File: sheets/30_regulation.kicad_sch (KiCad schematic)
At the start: 25 parts, among them U301 TPS62A02QDRLRQ1, U302 LP5907QMFX-3.3Q1

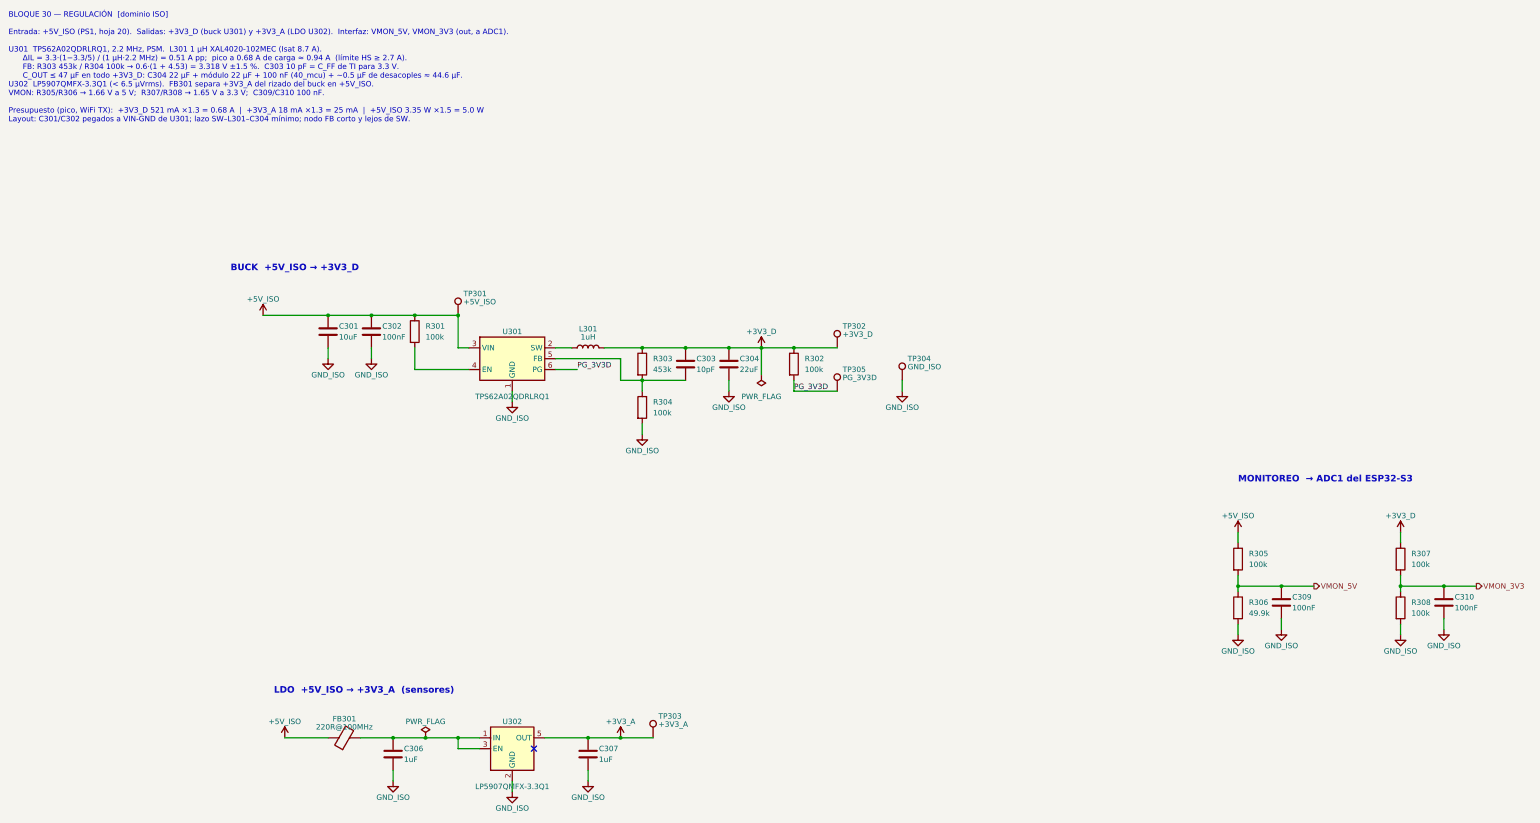
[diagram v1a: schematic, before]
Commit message: [Claude Code] 20_buck_5v: opción B (no aislada) con LMR38010; masas unificadas
- sheets/20_isolation -> sheets/20_buck_5v: se quitan PS201, ISO7763 y
  TPS7A1650; U201 LMR38010SQDDARQ1 (PROTO: LMR38010SDDAR, LCSC C5219310),
  5.02 V / 1 A a 400 kHz según TI SNVSC73B (L201 XAL6060-333, 3 x 22 uF,
  RT 64.9k, FB 100k/24.9k). Huella oficial HSOIC-8 con vías térmicas.
- Símbolo LMR38010 (easyeda2kicad) en lib/easyeda2kicad/INCLI-VA_easyeda,
  con tipos de pin ajustados; registrado en sym-lib-table.
- Todas las hojas: GND_ISO -> GND_VEH, +5V_ISO -> +5V_VEH.
- Raíz: EN/DIAG/FLT directos entre las hojas 40, 70 y 10; la hoja 20 sin pines.
- 10_power_input: R111 a +3V3_D, C109 = 100 nF (inrush con C105),
  C105 DNP solo en PROTO; se quita un PWR_FLAG suelto en GND_VEH.
- 70_output_ch: cambios de layout del usuario (hechos en KiCad).
- Textos de las hojas 30/40/50/80 y la raíz sin referencias al aislamiento.
- ERC: 0 en 10, 20, 30, 40, 50, 60 y 70; quedan los de 80 (hoja vacía).

Co-Authored-By: Claude Opus 5.5 <noreply@anthropic.com>
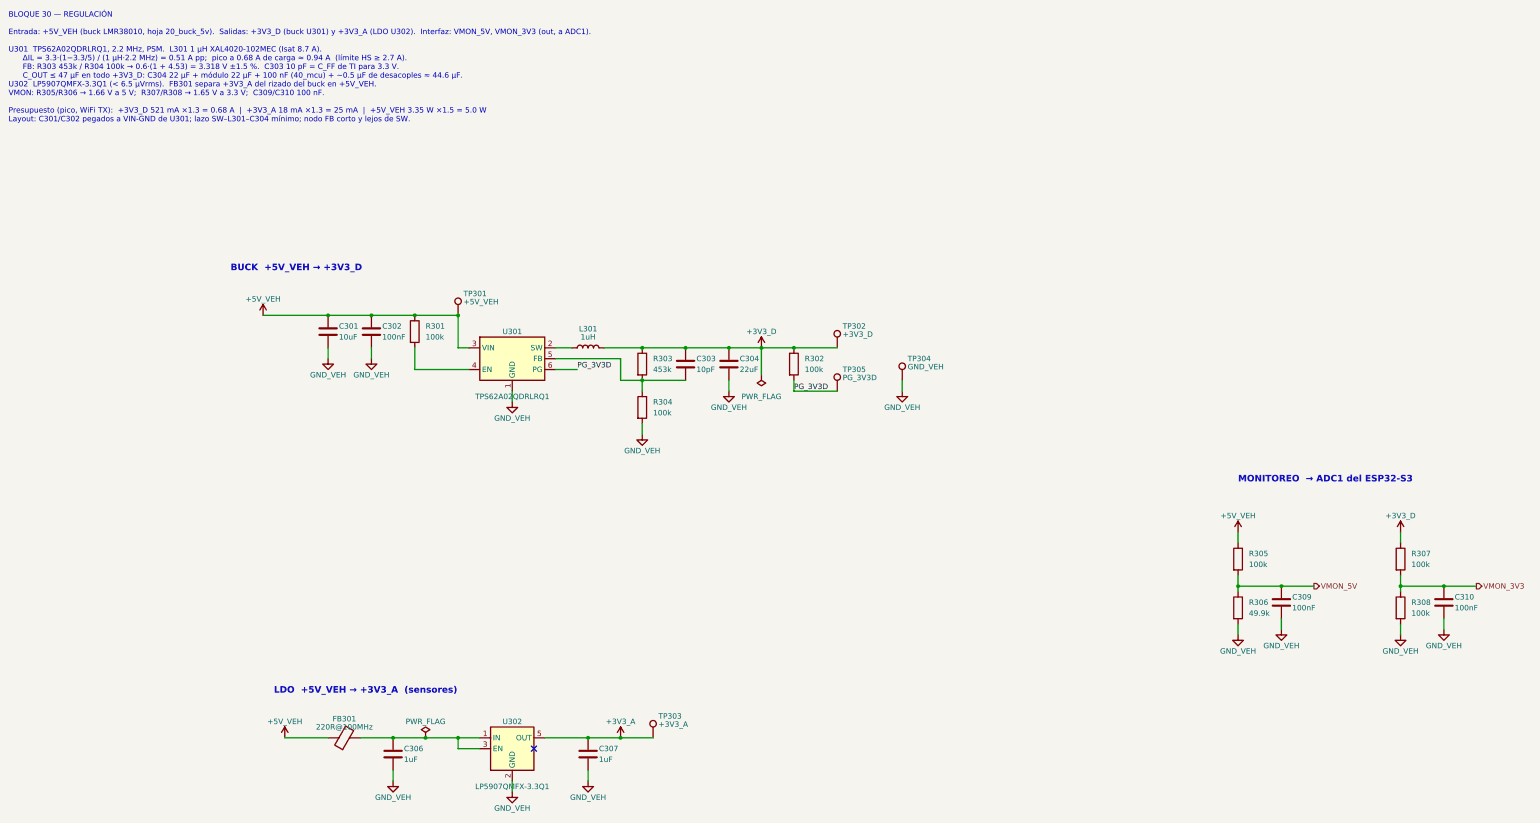
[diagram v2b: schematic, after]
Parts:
- FB301: Notes Aísla la entrada del LDO del rizado que el buck inyecta en +5V_ISO. 1.4 A, ~25 mA de carga. MPN a verificar (disponibilidad y especificación) antes de congelar el BOM. -> Aísla la entrada del LDO del rizado que el buck inyecta en +5V_VEH. 1.4 A, ~25 mA de carga. MPN a verificar (disponibilidad y especificación) antes de congelar el BOM.
- R301: Notes EN de U301 a +5V_ISO: el buck arranca con el riel (EN no pu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 -> EN de U301 a +5V_VEH: el buck arranca con el riel (EN no pu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
- TP301: value +5V_ISO -> +5V_VEH
- TP304: value GND_ISO -> GND_VEH
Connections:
- net +5V_ISO renamed +5V_VEH
- net GND_ISO renamed GND_VEH
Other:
- note added: "BLOQUE 30 — REGULACIÓN Entrada: +5V_VEH (buck LMR38010, hoja 20_buck_5v). Salidas: +3V3_D (buck U301) y +3V3_A (LDO U302). Interfaz: VMON_5V, VMON_3V3 (out, a ADC1). U301 TPS62A02QDRLRQ1, 2.2 MHz, PSM. L301 1 µH XAL4020-102MEC (Isat 8.7 A). ΔIL = 3.3·(1−3.3/5) / (1 µH·2.2 MHz) = 0.51 A pp; pico a 0.68 A de carga ≈ 0.94 A (límite HS ≥ 2.7 A). FB: R303 453k / R304 100k → 0.6·(1 + 4.53) = 3.318 V ±1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"
- note added: "BUCK +5V_VEH → +3V3_D"
- note added: "LDO +5V_VEH → +3V3_A (sensores)"
- note removed: "BLOQUE 30 — REGULACIÓN [dominio ISO] Entrada: +5V_ISO (PS1, hoja 20). Salidas: +3V3_D (buck U301) y +3V3_A (LDO U302). Interfaz: VMON_5V, VMON_3V3 (out, a ADC1). U301 TPS62A02QDRLRQ1, 2.2 MHz, PSM. L301 1 µH XAL4020-102MEC (Isat 8.7 A). ΔIL = 3.3·(1−3.3/5) / (1 µH·2.2 MHz) = 0.51 A pp; pico a 0.68 A de carga ≈ 0.94 A (límite HS ≥ 2.7 A). FB: R303 453k / R304 100k → 0.6·(1 + 4.53) = 3.318 V ±1.5 %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"
- note removed: "BUCK +5V_ISO → +3V3_D"
- note removed: "LDO +5V_ISO → +3V3_A (sensores)"
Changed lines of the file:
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@@
 		)
 	)
-	(text "LDO  +5V_ISO → +3V3_A  (sensores)"
+	(text "LDO  +5V_VEH → +3V3_A  (sensores)"
 		(exclude_from_sim no)
 		(at 82.55 180.34 0)
@@
 		)
 	)
-	(text "BUCK  +5V_ISO → +3V3_D"
+	(text "BUCK  +5V_VEH → +3V3_D"
 		(exclude_from_sim no)
 		(at 72.39 81.28 0)
@@
 		)
 	)
-	(text "BLOQUE 30 — REGULACIÓN  [dominio ISO]\n\nEntrada: +5V_ISO (PS1, hoja 20).  Salidas: +3V3_D (buck U301) y +3V3_A (LDO U302).  Interfaz: VMON_5V, VMON_3V3 (out, a ADC1).\n\nU301  TPS62A02QDRLRQ1, 2.2 MHz, PSM.  L301 1 µH XAL4020-102MEC (Isat 8.7 A).\n      ΔIL = 3.3·(1−3.3/5) / (1 µH·2.2 MHz) = 0.51 A pp;  pico a 0.68 A de carga ≈ 0.94 A  (límite HS ≥ 2.7 A).\n      FB: R303 453k / R304 100k → 0.6·(1 + 4.53) = 3.318 V ±1.5 %.  C303 10 pF = C_FF de TI para 3.3 V.\n      C_OUT ≤ 47 µF en todo +3V3_D: C304 22 µF + módulo 22 µF + 100 nF (40_mcu) + ~0.5 µF de desacoples ≈ 44.6 µF.\nU302  LP5907QMFX-3.3Q1 (< 6.5 µVrms).  FB301 separa +3V3_A del rizado del buck en +5V_ISO.\nVMON: R305/R306 → 1.66 V a 5 V;  R307/R308 → 1.65 V a 3.3 V;  C309/C310 100 nF.\n\nPresupuesto (pico, WiFi TX):  +3V3_D 521 mA ×1.3 = 0.68 A  |  +3V3_A 18 mA ×1.3 = 25 mA  |  +5V_ISO 3.35 W ×1.5 = 5.0 W\nLayout: C301/C302 pegados a VIN-GND de U301; lazo SW–L301–C304 mínimo; nodo FB corto y lejos de SW."
+	(text "BLOQUE 30 — REGULACIÓN\n\nEntrada: +5V_VEH (buck LMR38010, hoja 20_buck_5v).  Salidas: +3V3_D (buck U301) y +3V3_A (LDO U302).  Interfaz: VMON_5V, VMON_3V3 (out, a ADC1).\n\nU301  TPS62A02QDRLRQ1, 2.2 MHz, PSM.  L301 1 µH XAL4020-102MEC (Isat 8.7 A).\n      ΔIL = 3.3·(1−3.3/5) / (1 µH·2.2 MHz) = 0.51 A pp;  pico a 0.68 A de carga ≈ 0.94 A  (límite HS ≥ 2.7 A).\n      FB: R303 453k / R304 100k → 0.6·(1 + 4.53) = 3.318 V ±1.5 %.  C303 10 pF = C_FF de TI para 3.3 V.\n      C_OUT ≤ 47 µF en todo +3V3_D: C304 22 µF + módulo 22 µF + 100 nF (40_mcu) + ~0.5 µF de desacoples ≈ 44.6 µF.\nU302  LP5907QMFX-3.3Q1 (< 6.5 µVrms).  FB301 separa +3V3_A del rizado del buck en +5V_VEH.\nVMON: R305/R306 → 1.66 V a 5 V;  R307/R308 → 1.65 V a 3.3 V;  C309/C310 100 nF.\n\nPresupuesto (pico, WiFi TX):  +3V3_D 521 mA ×1.3 = 0.68 A  |  +3V3_A 18 mA ×1.3 = 25 mA  |  +5V_VEH 3.35 W ×1.5 = 5.0 W\nLayout: C301/C302 pegados a VIN-GND de U301; lazo SW–L301–C304 mínimo; nodo FB corto y lejos de SW."
 		(exclude_from_sim no)
 		(at 20.32 20.32 0)
@@
 	)
 	(symbol
-		(lib_id "INCLI-VA:GND_ISO")
+		(lib_id "INCLI-VA:GND_VEH")
 		(at 189.23 109.22 0)
 		(unit 1)
@@
 			)
 		)
-		(property "Value" "GND_ISO"
+		(property "Value" "GND_VEH"
 			(at 189.23 113.03 0)
 			(show_name no)
@@
 	)
 	(symbol
-		(lib_id "INCLI-VA:GND_ISO")
+		(lib_id "INCLI-VA:GND_VEH")
 		(at 229.87 109.22 0)
 		(unit 1)
@@
 			)
 		)
-		(property "Value" "GND_ISO"
+		(property "Value" "GND_VEH"
 			(at 229.87 113.03 0)
 			(show_name no)
@@
 	)
 	(symbol
-		(lib_id "INCLI-VA:+5V_ISO")
+		(lib_id "INCLI-VA:+5V_VEH")
 		(at 80.01 91.44 0)
 		(unit 1)
@@
 			)
 		)
-		(property "Value" "+5V_ISO"
+		(property "Value" "+5V_VEH"
 			(at 80.01 87.63 0)
 			(show_name no)
@@
 	)
 	(symbol
-		(lib_id "INCLI-VA:GND_ISO")
+		(lib_id "INCLI-VA:GND_VEH")
 		(at 138.43 111.76 0)
 		(unit 1)
@@
 			)
 		)
-		(property "Value" "GND_ISO"
+		(property "Value" "GND_VEH"
 			(at 138.43 115.57 0)
 			(show_name no)
@@
 	)
 	(symbol
-		(lib_id "INCLI-VA:GND_ISO")
+		(lib_id "INCLI-VA:GND_VEH")
 		(at 95.25 101.6 0)
 		(unit 1)
@@
 			)
 		)
-		(property "Value" "GND_ISO"
+		(property "Value" "GND_VEH"
 			(at 95.25 105.41 0)
 			(show_name no)
@@
 	)
 	(symbol
-		(lib_id "INCLI-VA:GND_ISO")
+		(lib_id "INCLI-VA:GND_VEH")
 		(at 168.91 119.38 0)
 		(unit 1)
@@
 			)
 		)
-		(property "Value" "GND_ISO"
+		(property "Value" "GND_VEH"
 			(at 168.91 123.19 0)
 			(show_name no)
@@
 	)
 	(symbol
-		(lib_id "INCLI-VA:GND_ISO")
+		(lib_id "INCLI-VA:GND_VEH")
 		(at 156.21 200.66 0)
 		(unit 1)
@@
 			)
 		)
-		(property "Value" "GND_ISO"
+		(property "Value" "GND_VEH"
 			(at 156.21 204.47 0)
 			(show_name no)
@@
 	)
 	(symbol
-		(lib_id "INCLI-VA:GND_ISO")
+		(lib_id "INCLI-VA:GND_VEH")
 		(at 356.87 165.1 0)
 		(unit 1)
@@
 			)
 		)
-		(property "Value" "GND_ISO"
+		(property "Value" "GND_VEH"
 			(at 356.87 168.91 0)
 			(show_name no)
@@
 	)
 	(symbol
-		(lib_id "INCLI-VA:+5V_ISO")
+		(lib_id "INCLI-VA:+5V_VEH")
 		(at 85.09 190.5 0)
 		(unit 1)
@@
 			)
 		)
-		(property "Value" "+5V_ISO"
+		(property "Value" "+5V_VEH"
 			(at 85.09 186.69 0)
 			(show_name no)
@@
 			)
 		)
-		(property "Value" "GND_ISO"
+		(property "Value" "GND_VEH"
 			(at 231.14 103.51 0)
 			(show_name no)
@@
 	)
 	(symbol
-		(lib_id "INCLI-VA:GND_ISO")
+		(lib_id "INCLI-VA:GND_VEH")
 		(at 318.77 165.1 0)
 		(unit 1)
@@
 			)
 		)
-		(property "Value" "GND_ISO"
+		(property "Value" "GND_VEH"
 			(at 318.77 168.91 0)
 			(show_name no)
@@
 			)
 		)
-		(property "Notes" "EN de U301 a +5V_ISO: el buck arranca con el riel (EN no puede quedar flotante, TI)."
+		(property "Notes" "EN de U301 a +5V_VEH: el buck arranca con el riel (EN no puede quedar flotante, TI)."
 			(at 115.57 95.25 0)
 			(hide yes)
@@
 			)
 		)
-		(property "Value" "+5V_ISO"
+		(property "Value" "+5V_VEH"
 			(at 127 88.27 0)
 			(show_name no)
@@
 	)
 	(symbol
-		(lib_id "INCLI-VA:GND_ISO")
+		(lib_id "INCLI-VA:GND_VEH")
 		(at 138.43 203.2 0)
 		(unit 1)
@@
 			)
 		)
-		(property "Value" "GND_ISO"
+		(property "Value" "GND_VEH"
 			(at 138.43 207.01 0)
 			(show_name no)
@@
 	)
 	(symbol
-		(lib_id "INCLI-VA:GND_ISO")
+		(lib_id "INCLI-VA:GND_VEH")
 		(at 105.41 101.6 0)
 		(unit 1)
@@
 			)
 		)
-		(property "Value" "GND_ISO"
+		(property "Value" "GND_VEH"
 			(at 105.41 105.41 0)
 			(show_name no)
@@
 			)
 		)
-		(property "Notes" "Aísla la entrada del LDO del rizado que el buck inyecta en +5V_ISO. 1.4 A, ~25 mA de carga. MPN a verificar (disponibilidad y especificación) antes de congelar el BOM."
+		(property "Notes" "Aísla la entrada del LDO del rizado que el buck inyecta en +5V_VEH. 1.4 A, ~25 mA de carga. MPN a verificar (disponibilidad y especificación) antes de congelar el BOM."
 			(at 99.06 190.5 0)
 			(hide yes)
@@
 	)
 	(symbol
-		(lib_id "INCLI-VA:GND_ISO")
+		(lib_id "INCLI-VA:GND_VEH")
 		(at 346.71 166.37 0)
 		(unit 1)
@@
 			)
 		)
-		(property "Value" "GND_ISO"
+		(property "Value" "GND_VEH"
 			(at 346.71 170.18 0)
 			(show_name no)
@@
 	)
 	(symbol
-		(lib_id "INCLI-VA:GND_ISO")
+		(lib_id "INCLI-VA:GND_VEH")
 		(at 308.61 166.37 0)
 		(unit 1)
@@
 			)
 		)
-		(property "Value" "GND_ISO"
+		(property "Value" "GND_VEH"
 			(at 308.61 170.18 0)
 			(show_name no)
@@
 	)
 	(symbol
-		(lib_id "INCLI-VA:GND_ISO")
+		(lib_id "INCLI-VA:GND_VEH")
 		(at 110.49 200.66 0)
 		(unit 1)
@@
 			)
 		)
-		(property "Value" "GND_ISO"
+		(property "Value" "GND_VEH"
 			(at 110.49 204.47 0)
 			(show_name no)
@@
 	)
 	(symbol
-		(lib_id "INCLI-VA:+5V_ISO")
+		(lib_id "INCLI-VA:+5V_VEH")
 		(at 308.61 142.24 0)
 		(unit 1)
@@
 			)
 		)
-		(property "Value" "+5V_ISO"
+		(property "Value" "+5V_VEH"
 			(at 308.61 138.43 0)
 			(show_name no)
